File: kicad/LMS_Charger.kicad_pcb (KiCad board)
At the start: 2 copper layers, 18 x 15 mm, 20 parts, among them J1 USB4105-GF-A-120, J2 Cable Pad, J3 Cable Pad, J4 Cable Pad, J5 Cable Pad, Q1 DMP2165UW, U1 MCP73833-AMI

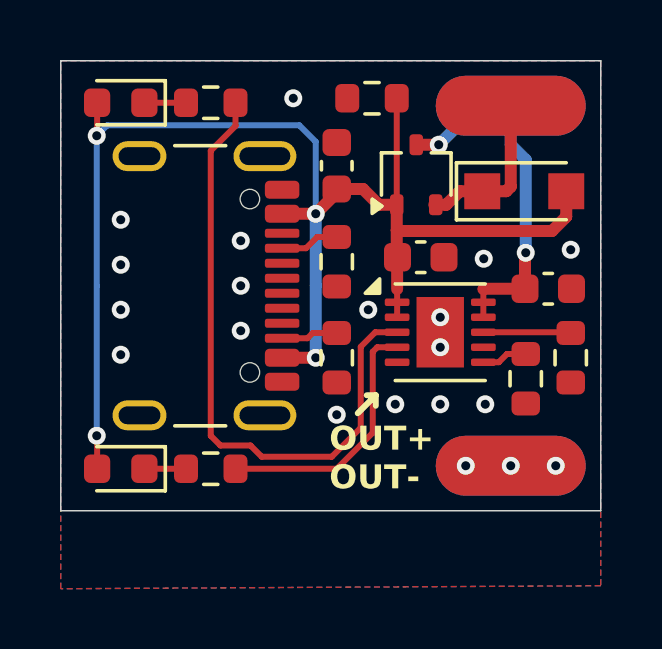
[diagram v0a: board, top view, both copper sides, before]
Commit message: feat(lower_current): Created light version of charger for small bateries
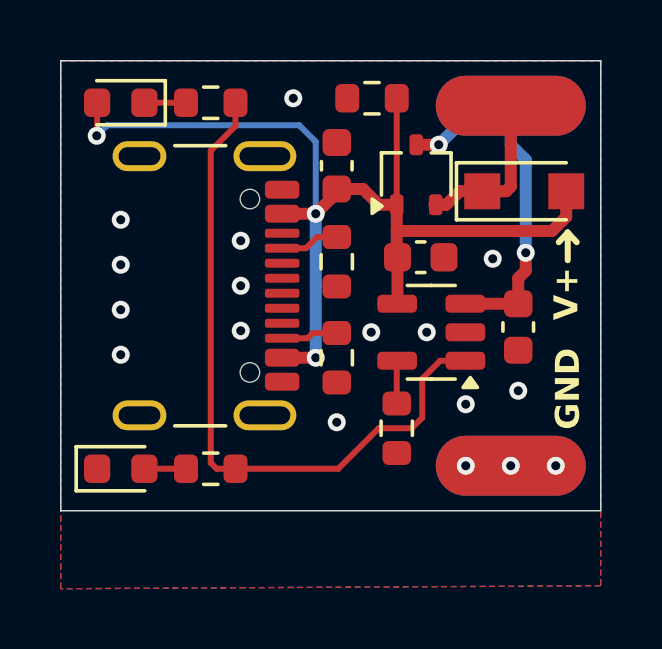
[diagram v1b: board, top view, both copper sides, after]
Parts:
- removed R7: NCU18XH103F60RB, Resistor_SMD:R_0603_1608Metric
- D3: value PMEG3020EH -> PMEG2010ER
- R4, R5: value 220R -> 470R
- U1: value MCP73833-AMI -> MCP73831-2ACI-OT; footprint Package_DFN_QFN:DFN-10-1EP_3x3mm_P0.5mm_EP1.58x2.35mm -> Package_TO_SOT_SMD:SOT-23-5
- moved R6 4.61 mm to (111.2, 99.8)
- moved C3 1.62 mm to (115.2, 96.4), turned to -90 degrees
- moved U1 0.30 mm to (112.3, 96.5), turned to 180 degrees
- turned D2 to 0 degrees
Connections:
- D2 pad 1: Net-(D2-K) -> GNDD
- D2 pad 2: +5V -> Net-(D2-A)
- R4 pad 2: Net-(U1-STAT1) -> Net-(U1-STAT)
- R5 pad 1: Net-(D2-K) -> Net-(D2-A)
- R5 pad 2: Net-(U1-STAT2) -> Net-(U1-STAT)
- U1 pad 1: +5V -> Net-(U1-STAT)
- U1 pad 2: +5V -> GNDD
- U1 pad 3: Net-(U1-STAT1) -> +BATT
- U1 pad 4: Net-(U1-STAT2) -> +5V
- U1 pad 5: GNDD -> Net-(U1-PROG)
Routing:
- net Net-(U1-STAT): track 0.00 -> 23.2 mm
- net Net-(U1-STAT1): track 21.2 -> 0.00 mm
- net +5V: track 46.7 -> 35.1 mm, vias 4 -> 3
- net Net-(U1-STAT2): track 8.65 -> 0.00 mm
- net Net-(U1-THERM): track 2.92 -> 0.00 mm
- net Net-(D2-K): track 1.39 -> 0.00 mm
- net Net-(D2-A): track 0.00 -> 1.39 mm
- net GNDD: vias 20 -> 17
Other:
- board text added: "GND"
- board text added: "V+"
- board text removed: "OUT+ OUT-"

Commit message: fix(values): Minor updates in components and footprints
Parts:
- R6: value R_{prog} -> 2k2

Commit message: fix(power_path): Solved problem with leaking current through reverse diode, adjusted LED resistors
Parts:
- D3: value PMEG2010ER -> PMEG2010BER
- R4, R5: value 470R -> 1k
